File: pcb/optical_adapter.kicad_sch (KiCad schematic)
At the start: 25 parts, among them J1 Conn_01x06_Pin, Q1 BC847, Q2 BC847, Q3 BC857, Q5 IRLML2060, U1 LM1117MP-3.3

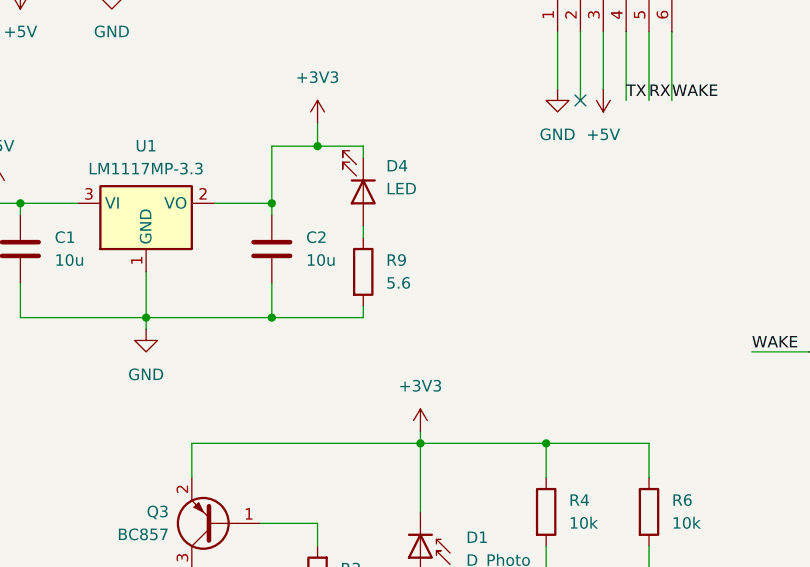
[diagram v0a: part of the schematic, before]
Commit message: Fix #1
Increase the value of the power LED resistor since the LED was to
bright.
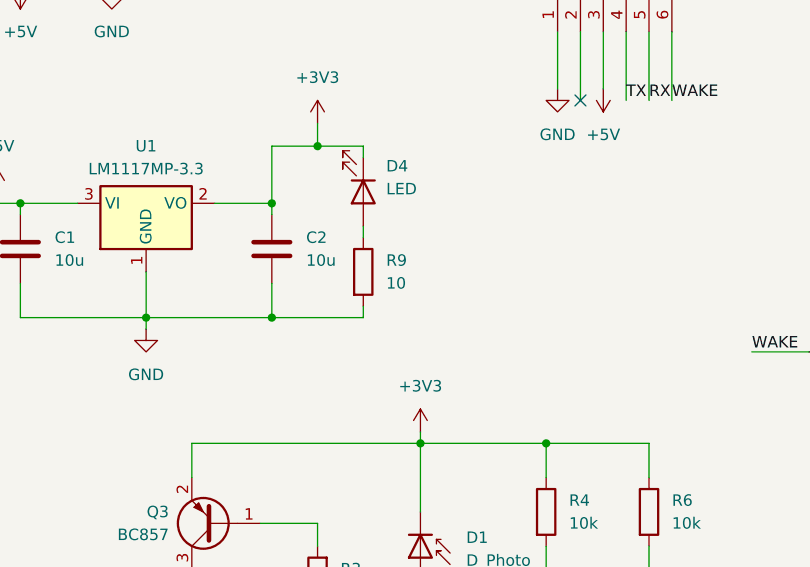
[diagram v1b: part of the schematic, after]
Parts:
- R9: value 5.6 -> 10; MFRNO CRCW12065R60JNEA -> CRCW120610R0JNEA; MOUSERNO 71-CRCW1206J-5.6-E3 -> 71-CRCW1206J-10-E3
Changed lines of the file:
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@@
 			)
 		)
-		(property "Value" "5.6"
+		(property "Value" "10"
 			(at 62.23 55.8799 0)
 			(effects
@@
 			)
 		)
-		(property "Datasheet" "https://www.vishay.com/doc?20035"
+		(property "Datasheet" "https://www.vishay.com/docs/20035/dcrcwe3.pdf"
 			(at 59.69 54.61 0)
 			(effects
@@
 			)
 		)
-		(property "MFRNO" "CRCW12065R60JNEA"
+		(property "MFRNO" " CRCW120610R0JNEA"
 			(at 59.69 54.61 0)
 			(effects
@@
 			)
 		)
-		(property "MOUSERNO" "71-CRCW1206J-5.6-E3 "
+		(property "MOUSERNO" "71-CRCW1206J-10-E3"
 			(at 59.69 54.61 0)
 			(effects

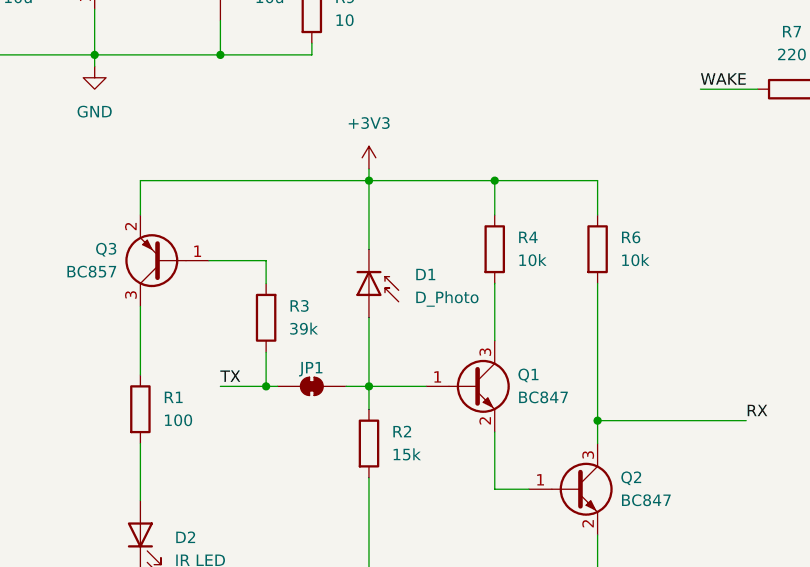
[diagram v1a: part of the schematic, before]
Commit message: Fix #5
Change D1 to Q4(phototransistor)
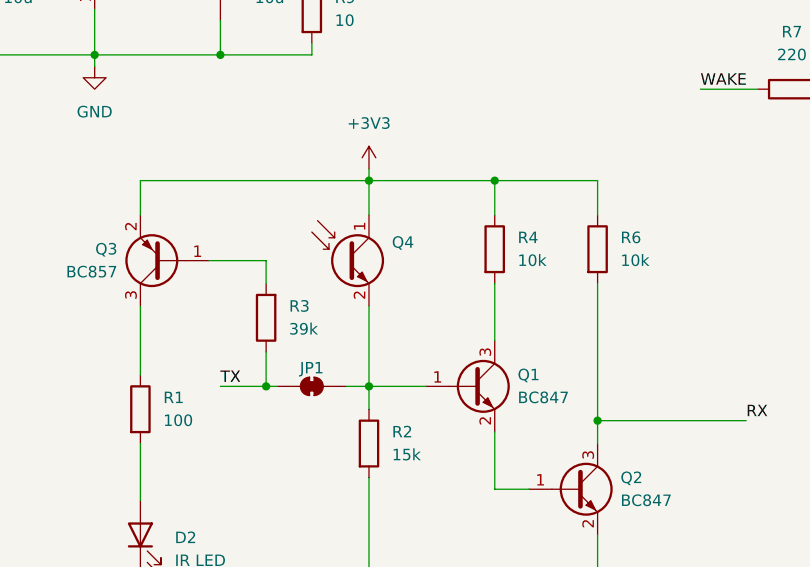
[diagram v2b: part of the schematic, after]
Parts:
- removed D1: D_Photo, footprints:kingbright_heli_r, symbol Device:D_Photo
- added Q4: Q_Photo_NPN, footprints:kingbright_heli_r, symbol Device:Q_Photo_NPN
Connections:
- net +3V3: now also Q4.1 (C)
- net at JP1.2 (B), Q1.1 (B), R2.1: now also Q4.2 (E)
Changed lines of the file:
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@@
+	(wire
+		(pts
+			(xy 66.04 87.63) (xy 66.04 96.52)
+		)
+		(stroke
+			(width 0)
+			(type default)
+		)
+	)
 	(wire
 		(pts
@@
 	(wire
 		(pts
+			(xy 66.04 73.66) (xy 66.04 77.47)
+		)
+		(stroke
+			(width 0)
+			(type default)
+		)
+	)
+	(wire
+		(pts
 			(xy 91.44 85.09) (xy 91.44 100.33)
 		)
@@
 	(wire
 		(pts
-			(xy 66.04 73.66) (xy 66.04 81.28)
-		)
-		(stroke
-			(width 0)
-			(type default)
-		)
-	)
-	(wire
-		(pts
 			(xy 80.01 85.09) (xy 80.01 91.44)
-		)
-		(stroke
-			(width 0)
-			(type default)
-		)
-	)
-	(wire
-		(pts
-			(xy 66.04 88.9) (xy 66.04 96.52)
 		)
 		(stroke
@@
 				(path "/eed9174b-005f-42ed-94b9-b0e600055621"
 					(reference "#PWR013")
+					(unit 1)
+				)
+			)
+		)
+	)
+	(symbol
+		(lib_id "Device:Q_Photo_NPN")
+		(at 63.5 82.55 0)
+		(unit 1)
+		(exclude_from_sim no)
+		(in_bom yes)
+		(on_board yes)
+		(dnp no)
+		(fields_autoplaced yes)
+		(property "Reference" "Q4"
+			(at 68.58 80.5306 0)
+			(effects
+				(font
+					(size 1.27 1.27)
+				)
+				(justify left)
+			)
+		)
+		(property "Value" "Q_Photo_NPN"
+			(at 68.58 83.0706 0)
+			(effects
+				(font
+					(size 1.27 1.27)
+				)
+				(justify left)
+				(hide yes)
+			)
+		)
+		(property "Footprint" "footprints:kingbright_heli_r"
+			(at 68.58 80.01 0)
+			(effects
+				(font
+					(size 1.27 1.27)
+				)
+				(hide yes)
+			)
+		)
+		(property "Datasheet" "https://www.kingbrightusa.com/images/catalog/SPEC/APTR3216P3BT.pdf"
+			(at 63.5 82.55 0)
+			(effects
+				(font
+					(size 1.27 1.27)
+				)
+				(hide yes)
+			)
+		)
+		(property "Description" "NPN phototransistor, collector/emitter"
+			(at 63.5 82.55 0)
+			(effects
+				(font
+					(size 1.27 1.27)
+				)
+				(hide yes)
+			)
+		)
+		(property "LCSC" ""
+			(at 63.5 82.55 0)
+			(effects
+				(font
+					(size 1.27 1.27)
+				)
+				(hide yes)
+			)
+		)
+		(property "MFRNO" "APTR3216P3BT"
+			(at 63.5 82.55 0)
+			(effects
+				(font
+					(size 1.27 1.27)
+				)
+				(hide yes)
+			)
+		)
+		(property "MOUSERNO" "604-APTR3216P3BT"
+			(at 63.5 82.55 0)
+			(effects
+				(font
+					(size 1.27 1.27)
+				)
+				(hide yes)
+			)
+		)
+		(pin "2"
+		)
+		(pin "1"
+		)
+		(instances
+			(project ""
+				(path "/eed9174b-005f-42ed-94b9-b0e600055621"
+					(reference "Q4")
 					(unit 1)
 				)
@@
 					(unit 1)
 				)
-			)
-		)
-	)
-	(symbol
-		(lib_id "Device:D_Photo")
-		(at 66.04 86.36 270)
-		(unit 1)
-		(exclude_from_sim no)
-		(in_bom yes)
-		(on_board yes)
-		(dnp no)
-		(fields_autoplaced yes)
-		(property "Reference" "D1"
-			(at 71.12 84.1374 90)
-			(effects
-				(font
-					(size 1.27 1.27)
-				)
-				(justify left)
-			)
-		)
-		(property "Value" "D_Photo"
-			(at 71.12 86.6774 90)
-			(effects
-				(font
-					(size 1.27 1.27)
-				)
-				(justify left)
-			)
-		)
-		(property "Footprint" "footprints:kingbright_heli_r"
-			(at 66.04 85.09 0)
-			(effects
-				(font
-					(size 1.27 1.27)
-				)
-				(hide yes)
-			)
-		)
-		(property "Datasheet" "https://www.kingbrightusa.com/images/catalog/SPEC/APTR3216P3BT.pdf"
-			(at 66.04 85.09 0)
-			(effects
-				(font
-					(size 1.27 1.27)
-				)
-				(hide yes)
-			)
-		)
-		(property "Description" "Photodiode"
-			(at 66.04 86.36 0)
-			(effects
-				(font
-					(size 1.27 1.27)
-				)
-				(hide yes)
-			)
-		)
-		(property "LCSC" ""
-			(at 66.04 86.36 0)
-			(effects
-				(font
-					(size 1.27 1.27)
-				)
-				(hide yes)
-			)
-		)
-		(property "MFRNO" "APTR3216P3BT"
-			(at 66.04 86.36 90)
-			(effects
-				(font
-					(size 1.27 1.27)
-				)
-				(hide yes)
-			)
-		)
-		(property "MOUSERNO" "604-APTR3216P3BT"
-			(at 66.04 86.36 90)
-			(effects
-				(font
-					(size 1.27 1.27)
-				)
-				(hide yes)
-			)
-		)
-		(pin "2"
-		)
-		(pin "1"
-		)
-		(instances
-			(project ""
-				(path "/eed9174b-005f-42ed-94b9-b0e600055621"
-					(reference "D1")
-					(unit 1)
-				)

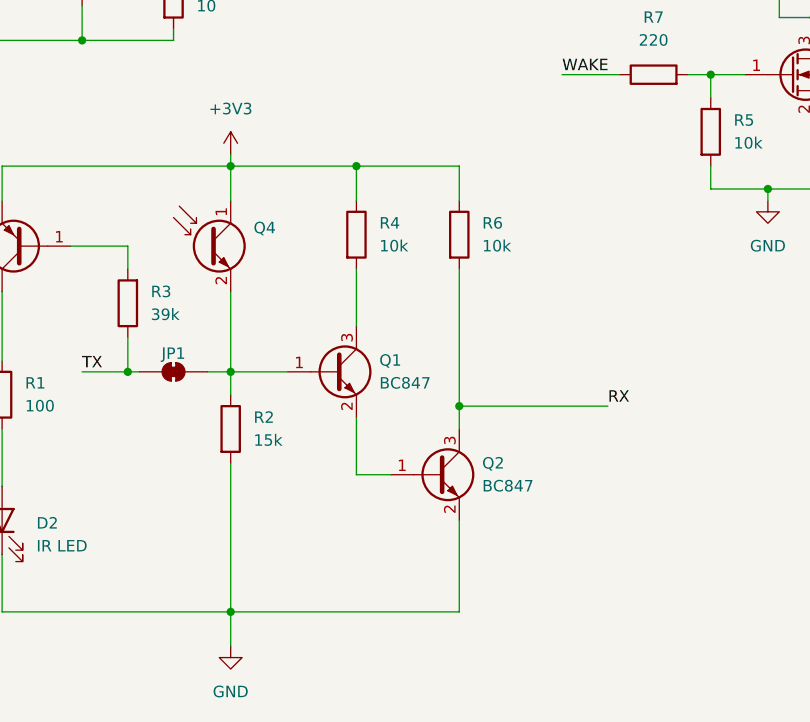
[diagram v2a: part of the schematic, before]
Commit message: Redesign RX circuit
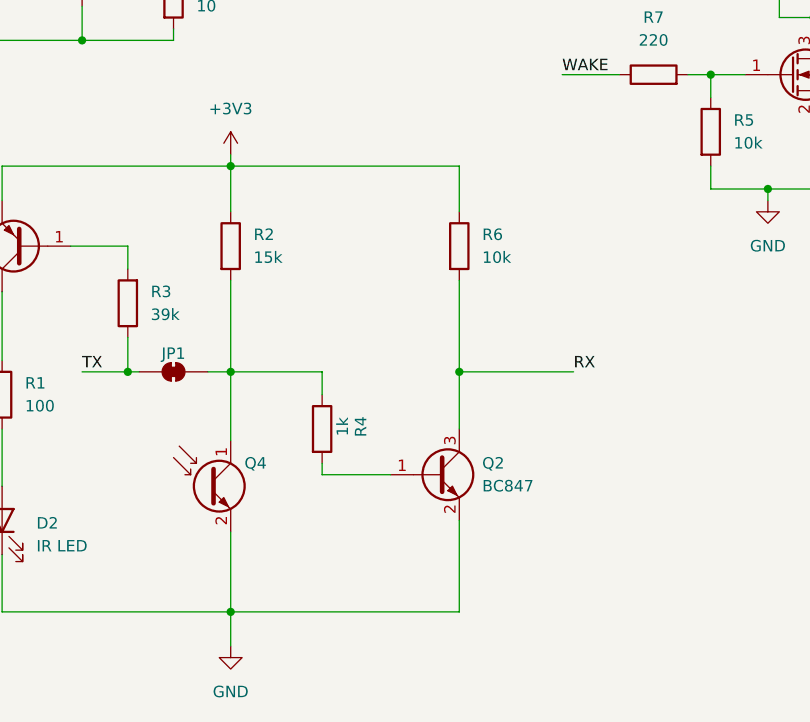
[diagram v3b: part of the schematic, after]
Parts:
- removed Q1: BC847, Package_TO_SOT_SMD:SOT-23, symbol Transistor_BJT:BC847
- R4: value 10k -> 1k; MFRNO CRCW120610K0JNEA -> CRCW120615K0JNEA; MOUSERNO 71-CRCW1206J-10K-E3 -> 71-CRCW1206J-15K-E3
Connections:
- net +3V3: now also R2.1; no longer Q4.1 (C), R4.1
- net GND: now also Q4.2 (E); no longer R2.2
- net at Q2.1 (B): now also R4.2
- new net: JP1.2 (B), Q4.1 (C), R2.2, R4.1
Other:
- moved on the sheet: Q4, R2, R6
